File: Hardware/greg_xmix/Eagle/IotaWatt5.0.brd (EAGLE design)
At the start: 80 x 118 mm, 66 parts, among them J0 2.1MMJACKSMT, J1 STEREO_SMD, J10 STEREO_SMD, J11 STEREO_SMD, J12 STEREO_SMD, J13 STEREO_SMD, J14 STEREO_SMD, J15 2.1MMJACKSMT, J16 2.1MMJACKSMT, J2 STEREO_SMD, J3 STEREO_SMD, J4 STEREO_SMD, J5 STEREO_SMD, J6 STEREO_SMD, J7 STEREO_SMD, J8 STEREO_SMD, J9 STEREO_SMD, Y1 32Khz

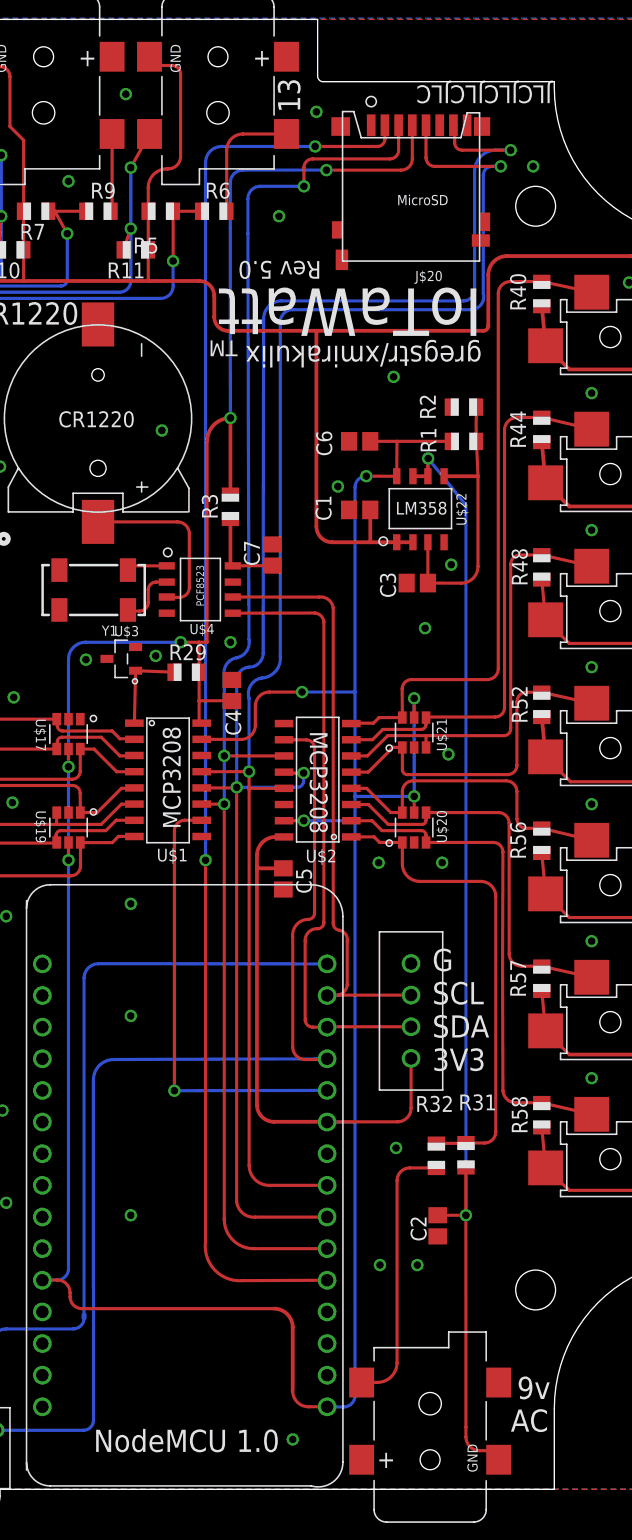
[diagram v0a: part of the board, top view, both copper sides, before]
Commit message: silkscreen upated
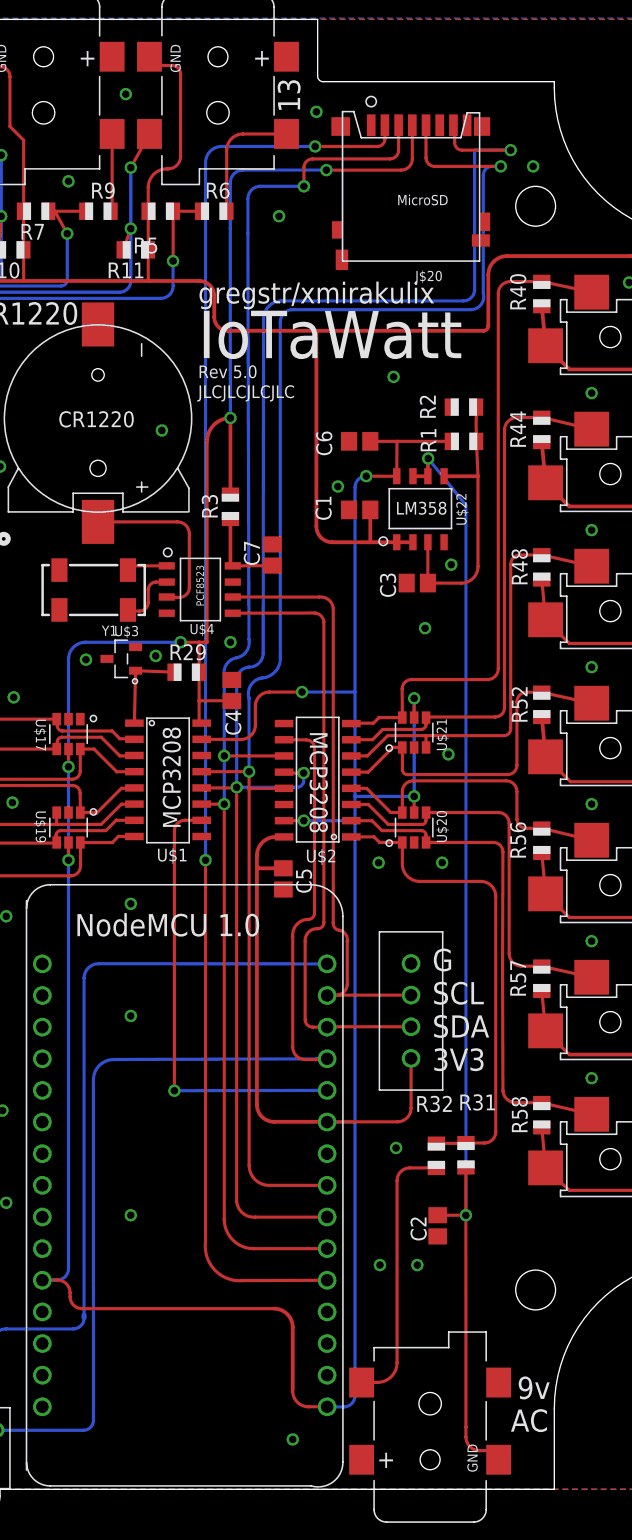
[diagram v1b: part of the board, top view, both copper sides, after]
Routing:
- net MISO: track 127.4 -> 128.4 mm
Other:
- board text removed: "TM"
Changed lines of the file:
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@@
 <drawing>
 <settings>
-<setting alwaysvectorfont="no"/>
+<setting alwaysvectorfont="yes"/>
 <setting keepoldvectorfont="yes"/>
 <setting verticaltext="up"/>
@@
 <wire x1="3" y1="18.5" x2="15" y2="6.5" width="0" layer="20" curve="-90"/>
 <wire x1="77" y1="18.5" x2="65" y2="6.5" width="0" layer="20" curve="90"/>
-<text x="79" y="22" size="1.778" layer="112" rot="R90">1</text>
-<text x="79" y="33" size="1.778" layer="112" rot="R90">2</text>
-<text x="79" y="44" size="1.778" layer="112" rot="R90">3</text>
-<text x="79" y="55" size="1.778" layer="112" rot="R90">4</text>
-<text x="79" y="66" size="1.778" layer="112" rot="R90">5</text>
-<text x="79" y="77" size="1.778" layer="112" rot="R90">6</text>
-<text x="79" y="88" size="1.778" layer="112" rot="R90">7</text>
-<text x="1" y="97" size="1.778" layer="112" rot="SR270">8</text>
-<text x="1" y="86" size="1.778" layer="112" rot="SR270">9</text>
-<text x="1" y="76" size="1.778" layer="112" rot="SR270">10</text>
-<text x="1" y="65" size="1.778" layer="112" rot="SR270">11</text>
-<text x="1" y="54.5" size="1.778" layer="112" rot="SR270">12</text>
-<text x="1" y="43.5" size="1.778" layer="112" rot="SR270">13</text>
-<text x="1" y="32.5" size="1.778" layer="112" rot="SR270">14</text>
-<text x="61.5" y="4.625" size="1.778" layer="112">AC</text>
-<text x="62" y="7.25" size="1.778" layer="112">9v</text>
-<text x="28" y="3" size="1.778" layer="112">NodeMCU 1.0</text>
-<text x="35" y="53" size="1.4224" layer="112" rot="R90">MCP3208</text>
-<text x="45.375" y="60.875" size="1.4224" layer="112" rot="SR270">MCP3208</text>
-<text x="36.875" y="70.875" size="0.6096" layer="112" rot="R90">PCF8523</text>
-<text x="46.3" y="98.6" size="1.4224" layer="112" rot="SR180">Rev 5.0</text>
-<text x="52.25" y="78.25" size="1.016" layer="112">LM358</text>
+<text x="79" y="22" size="1.778" layer="112" font="vector" rot="R90">1</text>
+<text x="79" y="33" size="1.778" layer="112" font="vector" rot="R90">2</text>
+<text x="79" y="44" size="1.778" layer="112" font="vector" rot="R90">3</text>
+<text x="79" y="55" size="1.778" layer="112" font="vector" rot="R90">4</text>
+<text x="79" y="66" size="1.778" layer="112" font="vector" rot="R90">5</text>
+<text x="79" y="77" size="1.778" layer="112" font="vector" rot="R90">6</text>
+<text x="79" y="88" size="1.778" layer="112" font="vector" rot="R90">7</text>
+<text x="1" y="97" size="1.778" layer="112" font="vector" rot="SR270">8</text>
+<text x="1" y="86" size="1.778" layer="112" font="vector" rot="SR270">9</text>
+<text x="1" y="76" size="1.778" layer="112" font="vector" rot="SR270">10</text>
+<text x="1" y="65" size="1.778" layer="112" font="vector" rot="SR270">11</text>
+<text x="1" y="54.5" size="1.778" layer="112" font="vector" rot="SR270">12</text>
+<text x="1" y="43.5" size="1.778" layer="112" font="vector" rot="SR270">13</text>
+<text x="1" y="32.5" size="1.778" layer="112" font="vector" rot="SR270">14</text>
+<text x="61.5" y="4.625" size="1.778" layer="112" font="vector">AC</text>
+<text x="62" y="7.25" size="1.778" layer="112" font="vector">9v</text>
+<text x="26.5" y="44.4" size="1.778" layer="112" font="vector">NodeMCU 1.0</text>
+<text x="35" y="53" size="1.4224" layer="112" font="vector" rot="R90">MCP3208</text>
+<text x="45.375" y="60.875" size="1.4224" layer="112" font="vector" rot="SR270">MCP3208</text>
+<text x="36.875" y="70.875" size="0.6096" layer="112" font="vector" rot="R90">PCF8523</text>
+<text x="36.4" y="89.201996875" size="1.016" layer="112" font="vector" rot="SR0">Rev 5.0</text>
+<text x="52.25" y="78.25" size="1.016" layer="112" font="vector">LM358</text>
 <circle x="20.8" y="76.3" radius="0.360553125" width="0.4064" layer="21"/>
-<text x="59.2" y="96.4" size="3.81" layer="112" rot="SR180">IoTaWatt</text>
-<text x="39.565" y="92.23" size="1.27" layer="112" rot="SR180">TM</text>
-<text x="86.7" y="56.2" size="1.6764" layer="121">(c)Copyright 2019, IoTaWatt, Inc.
+<text x="36.4" y="90.80399375" size="3.81" layer="112" font="vector" rot="SR0">IoTaWatt</text>
+<text x="86.7" y="56.2" size="1.6764" layer="121" font="vector">(c)Copyright 2019, IoTaWatt, Inc.
 IoTaWatt is a trademark of IoTaWatt, Inc.
 This work is licensed under the Creative Commons 4.0
@@
 <wire x1="46" y1="113.5" x2="46" y2="118" width="0" layer="20"/>
 <wire x1="46" y1="113.5" x2="46.5" y2="113" width="0" layer="20" curve="102.680383"/>
-<text x="44.6" y="110.5" size="1.778" layer="112" rot="SR90">13</text>
-<text x="19" y="110.5" size="1.778" layer="112" rot="R90">14</text>
-<text x="55.2" y="33.6" size="1.778" layer="112">G
+<text x="44.6" y="110.5" size="1.778" layer="112" font="vector" rot="SR90">13</text>
+<text x="19" y="110.5" size="1.778" layer="112" font="vector" rot="R90">14</text>
+<text x="55.2" y="33.6" size="1.778" layer="112" font="vector">G
 SCL
 SDA
 3V3</text>
-<text x="18.2" y="93.5" size="1.778" layer="112">CR1220</text>
-<text x="59.2" y="91.8" size="1.6764" layer="112" rot="SR180">gregstr/xmirakulix</text>
-<text x="64.8" y="112.7" size="1.4224" layer="112" rot="SR180">JLCJLCJLCJLC</text>
+<text x="18.2" y="93.5" size="1.778" layer="112" font="vector">CR1220</text>
+<text x="36.4" y="95.199990625" size="1.6764" layer="112" font="vector" rot="SR0">gregstr/xmirakulix</text>
+<text x="36.4" y="87.6" size="1.016" layer="112" font="vector" rot="SR0">JLCJLCJLCJLC</text>
 </plain>
 <attributes>
@@
 <wire x1="43.1" y1="95.4" x2="57.7" y2="95.4" width="0.254" layer="16"/>
 <wire x1="57.7" y1="95.4" x2="58.6" y2="96.3" width="0.254" layer="16" curve="90"/>
-<wire x1="58.6" y1="96.3" x2="58.6" y2="105.8" width="0.254" layer="16"/>
-<wire x1="58.6" y1="105.8" x2="60.3" y2="107.5" width="0.254" layer="16" curve="-90"/>
-<wire x1="60.3" y1="107.5" x2="61.5" y2="107.5" width="0.254" layer="16"/>
+<wire x1="58.6" y1="96.3" x2="58.6" y2="107.5" width="0.254" layer="16"/>
+<wire x1="58.6" y1="107.5" x2="61.5" y2="107.5" width="0.254" layer="16"/>
 <via x="61.5" y="107.5" extent="1-16" drill="0.6"/>
 <wire x1="61.5" y1="107.5" x2="57.6" y2="107.5" width="0.254" layer="1"/>
